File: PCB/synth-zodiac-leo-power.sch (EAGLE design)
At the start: 29 parts, among them J1 2.5 ID x 5.5 OD, J2 HDR-02P

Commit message: Snapshot of designs so far.
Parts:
- removed J1: 2.5 ID x 5.5 OD, con-jack:DC-JACK-2.5MM-REGULAR
- removed J2: HDR-02P, con-headers:CON_02X1-2.54MM-THD-VT
- added 12V: HDR-02P, con-headers:CON_02X1-2.54MM-THD-VT
- added BOOST5: 5V Boost, regulators:BOOST-EN-POLOLU-5V
- added BOOST9, BOOST9N: BOOST 9V, regulators:BOOST-EN-POLOLU-9V
- added CONST: Leo, circuit-monkey-zodiac:CONSTELLATION-LEO
- added GLYPH: Leo, circuit-monkey-zodiac:GLYPH-LEO
- added PCB: PCB FAB, circuit-monkey-zodiac:PENTAGON-40R
- added PWR_AMP, PWR_COW, PWR_EG, PWR_KB, PWR_MIDI, PWR_VCA: (no value), con-jst:04P-VT-SMT
- added VBAT: 2-pin, VT, SMT, con-jst:02PVT-SMT
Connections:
- new net VBAT: VBAT.1
- net +5V: now also PWR_AMP.3, PWR_COW.3, PWR_EG.3, PWR_KB.3, PWR_MIDI.3, PWR_VCA.3
- net +9V: now also PWR_AMP.1, PWR_COW.1, PWR_EG.1, PWR_KB.1, PWR_MIDI.1, PWR_VCA.1
- net -9V: now also PWR_AMP.2, PWR_COW.2, PWR_EG.2, PWR_KB.2, PWR_MIDI.2, PWR_VCA.2
- net GND: now also 12V.2, PCB.GND@1, PWR_AMP.4, PWR_COW.4, PWR_EG.4, PWR_KB.4, PWR_MIDI.4, PWR_VCA.4, VBAT.2; no longer J1.GND, J2.2
- net N$1: now also 12V.1; no longer J1.VIN, J2.1
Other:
- note added: "TODO: - LI-Ion Batt charger - 12V Boost - LEDs - P.Switch Toggle (hole + pads)"
- moved on the sheet: C1, C10, C11, C2, C3, C4, C5, C6, C7, C8, C9, D1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

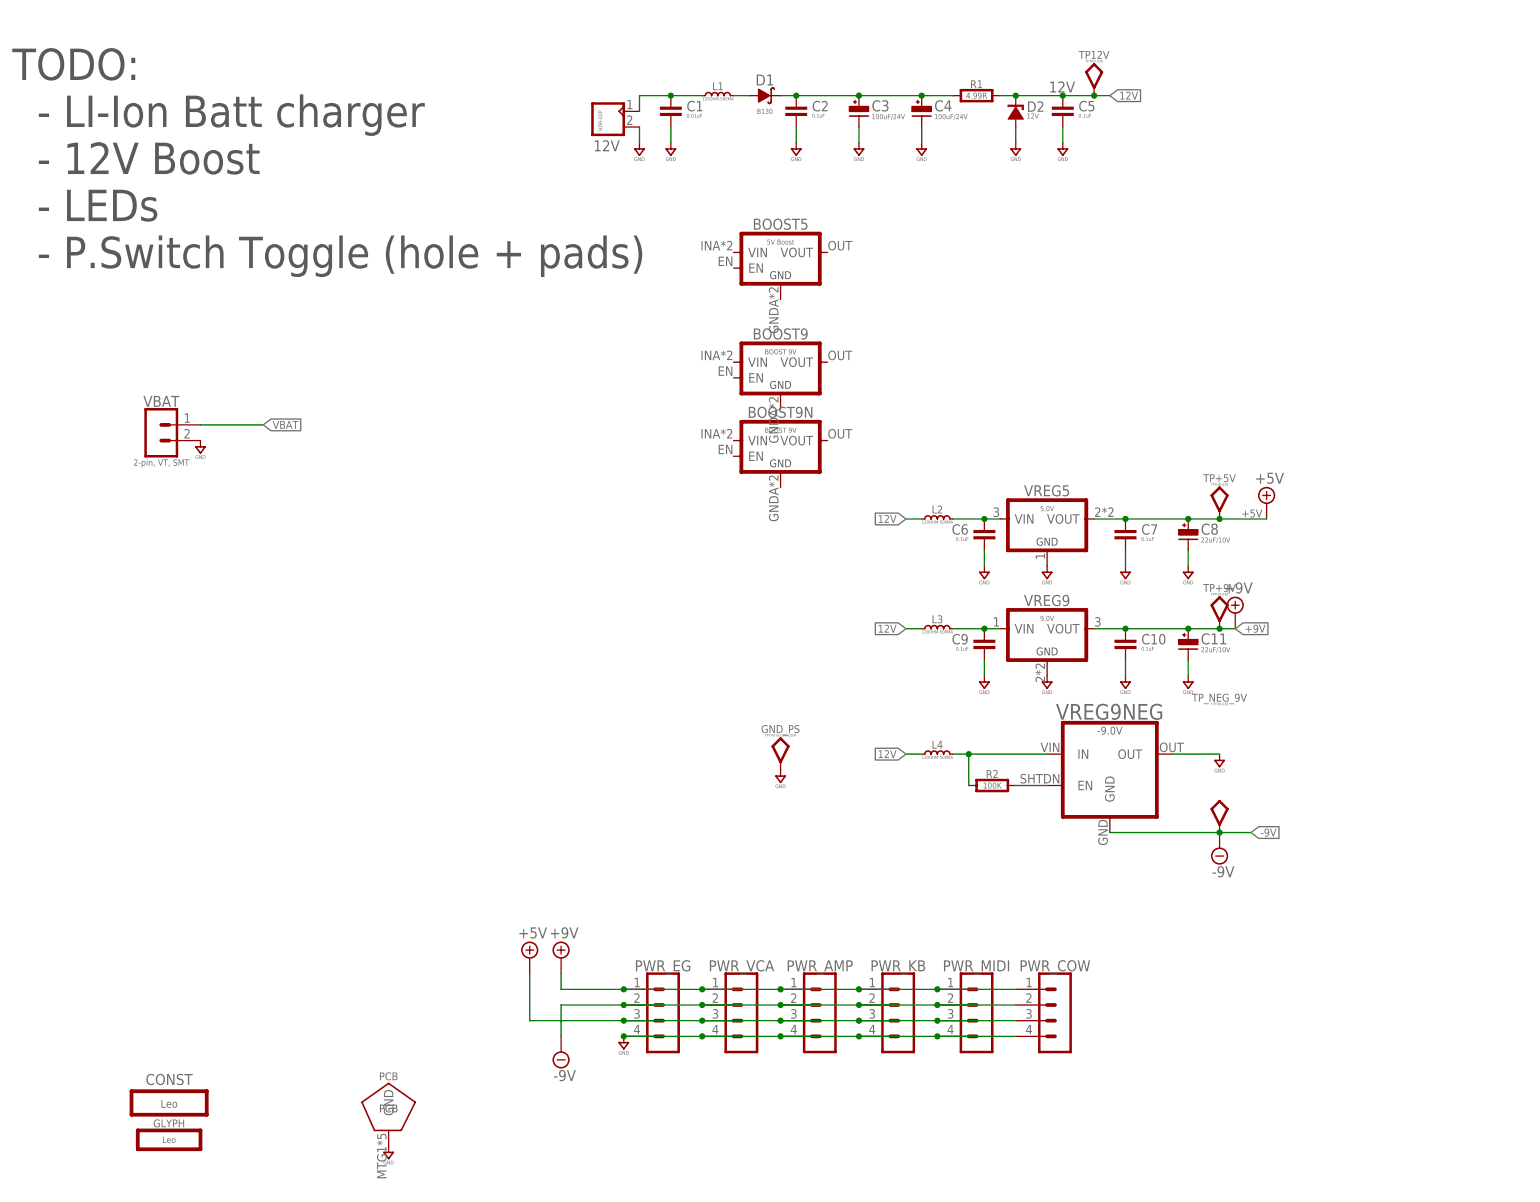
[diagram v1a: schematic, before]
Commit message: Almost ready for FAB.
Sagittarius was mis-spelled, renamed it.  Taurus is still WIP.
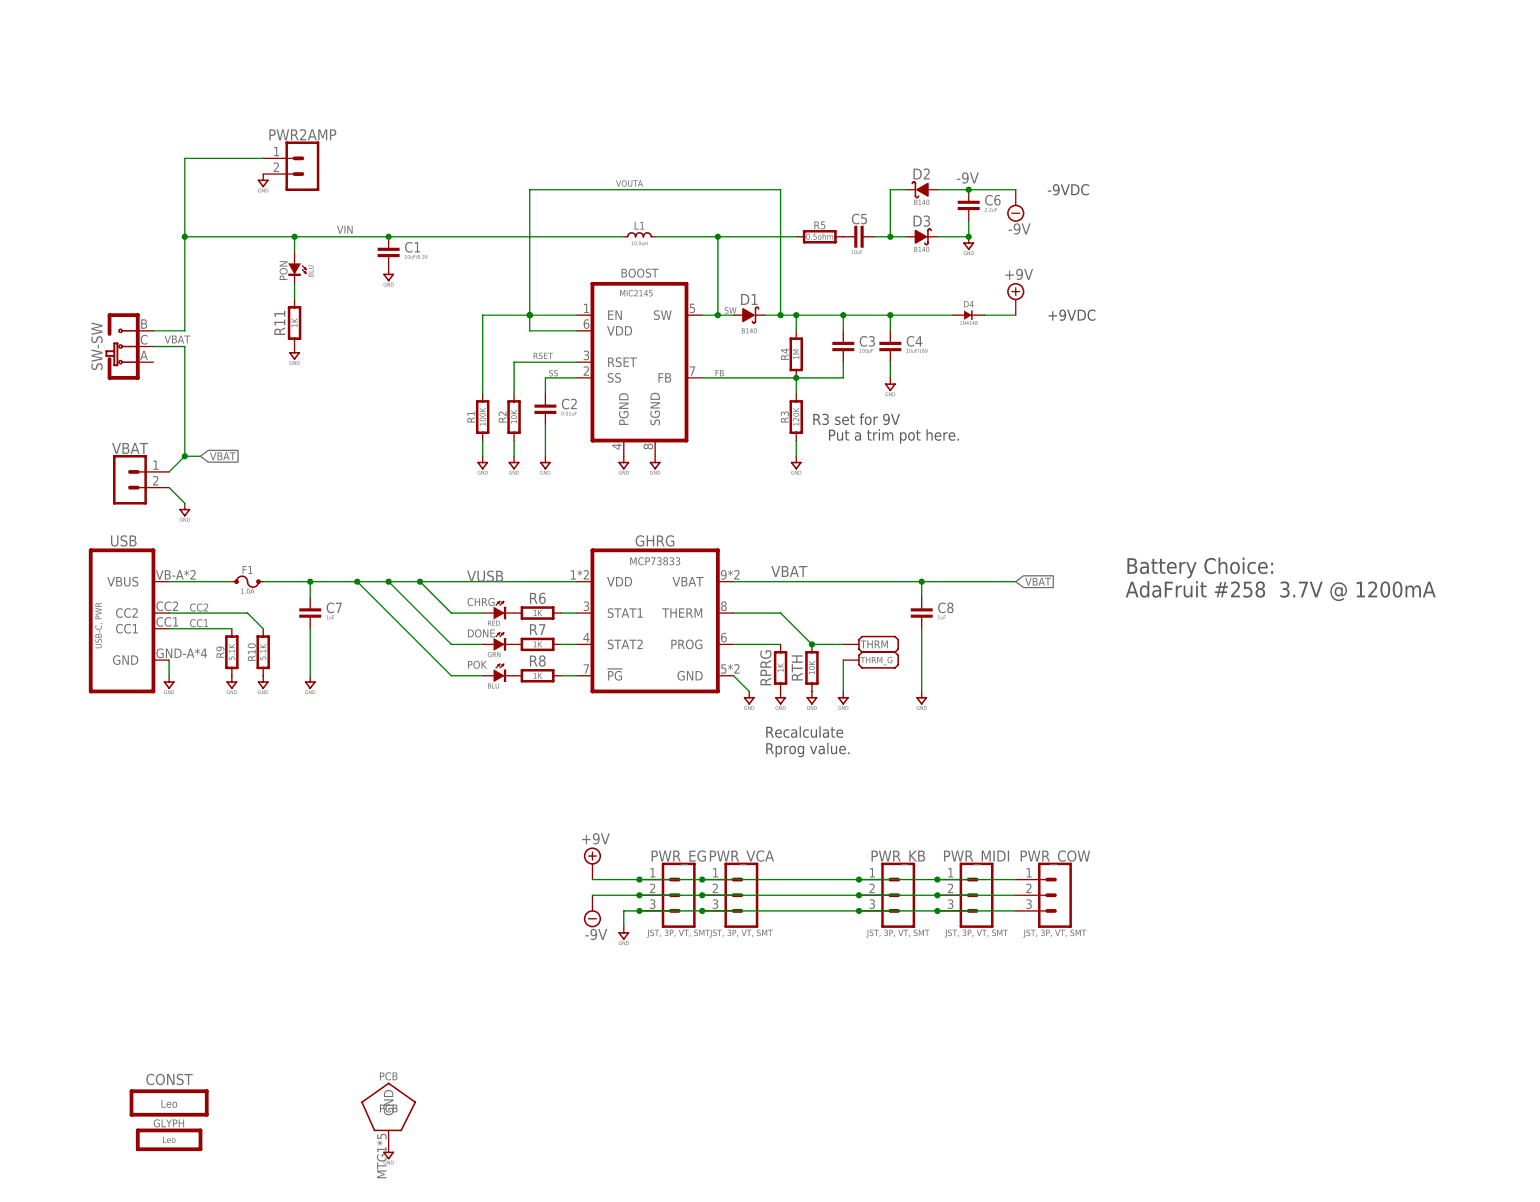
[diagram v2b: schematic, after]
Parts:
- removed 12V: HDR-02P, con-headers:CON_02X1-2.54MM-THD-VT
- removed BOOST5: 5V Boost, regulators:BOOST-EN-POLOLU-5V
- removed BOOST9, BOOST9N: BOOST 9V, regulators:BOOST-EN-POLOLU-9V
- removed C10, C9: 0.1uF, rlc:CAPACITOR0603
- removed C11: 22uF/10V, rlc:CAPACITOR_POL-ALUM-SMT-6.3
- removed GND_PS: TPTHD-SCOPE-LOOP, con-testpoints:TPTHD-SCOPE-LOOP
- removed L2, L3, L4: 120OHM-500MA, rlc:FERRITE120OHM-500MA
- removed PWR_AMP: (no value), con-jst:04P-VT-SMT
- removed TP+5V, TP+9V, TP12V, TP_NEG_9V: TPTHD-038, con-testpoints:TPTHD-038
- removed VREG5: 5.0V, regulators:LDO-3P-1117-5V
- removed VREG9: 9.0V, regulators:LDO-3P--9V
- removed VREG9NEG: -9.0V, regulators:POLOLU-STEPDOWN-4P-9.0V
- added BOOST: MIC2145, regulators:BOOST-MIC2145-MSOP
- added CHRG: RED, led:SMT0603
- added D3: B140, diodes:SCHOTTKYB140
- added D4: 1N4148, diodes:DIODE-1N4148
- added DONE: GRN, led:SMT0603
- added F1: 1.0A, fuse:FUSEBOURNS-MF-MSMF
- added GHRG: MCP73833, co-microchip:MCP73833-DFN
- added POK, PON: BLU, led:SMT0603
- added PWR2AMP: 2-pin, VT, SMT, con-jst:02PVT-SMT
- added R10, R9: 5.1K, rlc:RESISTOR0603
- added R11, R6, R7, R8, RPRG: 1K, rlc:RESISTOR0603
- added R3: 120K, rlc:RESISTOR0603
- added R4: 1M, rlc:RESISTOR0603
- added R5: 0.5ohm, rlc:RESISTOR0603
- added RTH: 10K, rlc:RESISTOR0603
- added SW: (no value), switch-thd:SLIDE-SPDTSS-12-F45-TH-PCB
- added THRM, THRM_G: PADSMD-050X050, con-testpoints:PADSMD-050X050
- added USB: USB-C, PWR, con-usb:USB-C-PWR-SMT-PNL
- C1: value 0.01uF -> 10uF/6.3V
- C2: value 0.1uF -> 0.01uF
- C3: value 100uF/24V -> 100pF; device rlc:CAPACITOR_POL-ALUM-SMT-6.3 -> rlc:CAPACITOR0603; COST01 0.5 -> (none); COST10 0.5 -> (none); COST100 0.4 -> (none); MFR Wurth -> (none); MPN 865090445008 -> (none)
- C4: value 100uF/24V -> 10uF/16V; device rlc:CAPACITOR_POL-ALUM-SMT-6.3 -> rlc:CAPACITOR0603; COST01 0.5 -> (none); COST10 0.5 -> (none); COST100 0.4 -> (none); MFR Wurth -> (none); MPN 865090445008 -> (none)
- C5: value 0.1uF -> 10uF
- C6: value 0.1uF -> 2.2uF
- C7: value 0.1uF -> 1uF
- C8: value 22uF/10V -> 1uF; device rlc:CAPACITOR_POL-ALUM-SMT-6.3 -> rlc:CAPACITOR0603; COST01 0.5 -> (none); COST10 0.5 -> (none); COST100 0.4 -> (none); MFR Wurth -> (none); MPN 865090445008 -> (none)
- D1: value B130 -> B140; device diodes:SCHOTTKYB130 -> diodes:SCHOTTKYB140
- D2: value 12V -> B140; device diodes:ZENERSOT-23 -> diodes:SCHOTTKYB140; COST01 0.44 -> (none); COST10 0.34 -> (none); COST100 0.20 -> (none); MFR ROHM -> (none); MPN BZX84B12VLYT116 -> (none)
- L1: value 120OHM-500MA -> 10.0uH; device rlc:FERRITE120OHM-500MA -> rlc:INDUCTORSMD-05X04MM; MPN BLM18SP102SN1D -> (none)
- PWR_COW, PWR_EG, PWR_KB, PWR_MIDI, PWR_VCA: value (none) -> JST, 3P, VT, SMT; device con-jst:04P-VT-SMT -> con-jst:03P-VT-SMT
- R1: value 4.99R -> 100K; device rlc:RESISTOR1206 -> rlc:RESISTOR0603
- R2: value 100K -> 10K
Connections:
- removed net +5V: C7.1, C8.P, PWR_AMP.3, PWR_COW.3, PWR_EG.3, PWR_KB.3, PWR_MIDI.3, PWR_VCA.3, TP+5V.P$1, VREG5.VOUT
- removed net 12V: C5.1, D2.K, L2.1, L3.1, L4.1, R1.2, TP12V.P$1
- new net CC1: R9.2, USB.CC1
- new net CC2: R10.2, USB.CC2
- new net FB: BOOST.FB, C3.2, R3.2, R4.1
- new net N$10: GHRG.STAT2, R7.2
- new net N$11: GHRG.!PG, R8.2
- new net N$12: GHRG.THERM, RTH.2, THRM.PAD
- new net N$8: GHRG.PROG, RPRG.2
- new net N$9: GHRG.STAT1, R6.2
- new net RSET: BOOST.RSET, R2.2
- new net SS: BOOST.SS, C2.1
- new net SW: BOOST.SW, D1.A, L1.P$1, R5.1
- new net VIN: C1.1, L1.P$2, PON.A, PWR2AMP.1, SW-SW.B
- new net VOUTA: BOOST.EN, BOOST.VDD, C3.1, C4.1, D1.K, D4.A, R1.2, R4.2
- new net VUSB: C7.1, CHRG.A, DONE.A, F1.2, GHRG.VDD, POK.A
- net +9V: now also D4.K; no longer C10.1, C11.P, PWR_AMP.1, TP+9V.P$1, VREG9.VOUT
- net -9V: now also C6.1, D2.A; no longer PWR_AMP.2, TP_NEG_9V.P$1, VREG9NEG.GND
- net GND: now also BOOST.PGND, BOOST.SGND, C4.2, C8.2, D3.K, GHRG.GND, PWR2AMP.2, PWR_COW.3, PWR_EG.3, PWR_KB.3, PWR_MIDI.3, PWR_VCA.3, R1.1, R10.1, R11.1, R2.1, R3.1, R9.1, RPRG.1, RTH.1, THRM_G.PAD, USB.GND; no longer 12V.2, C10.2, C11.N, C3.N, C4.N, C5.2, C8.N, C9.2, D2.A, GND_PS.P$1, PWR_AMP.4, PWR_COW.4, PWR_EG.4, PWR_KB.4, PWR_MIDI.4, PWR_VCA.4, VREG5.GND, VREG9.GND, VREG9NEG.OUT
- net N$1: now also C5.1, R5.2; no longer 12V.1, C1.1, L1.1
- net N$2: now also C5.2, D2.K, D3.A; no longer D1.A, L1.2
- net N$3: now also CHRG.C, R6.1; no longer C2.1, C3.P, C4.P, D1.K, R1.1
- net N$4: now also PON.C, R11.2; no longer C9.1, L3.2, VREG9.VIN
- net N$5: now also DONE.C, R7.1; no longer C6.1, L2.2, VREG5.VIN
- net N$6: now also F1.1, USB.VBUS; no longer L4.2, R2.1, VREG9NEG.IN
- net N$7: now also POK.C, R8.1; no longer R2.2, VREG9NEG.EN
- net VBAT: now also C8.1, GHRG.VBAT, SW-SW.C
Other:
- note added: "+9VDC"
- note added: "-9VDC"
- note added: "Battery Choice: AdaFruit #258 3.7V @ 1200mA"
- note added: "Put a trim pot here."
- note added: "R3 set for 9V"
- note added: "Recalculate Rprog value."
- note removed: "TODO: - LI-Ion Batt charger - 12V Boost - LEDs - P.Switch Toggle (hole + pads)"
- moved on the sheet: C1, C2, C5, C6, C7, D1, R1, R2, VBAT

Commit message: Work in progress for rev A,  VCO rev.B
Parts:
- removed PWR2AMP, VBAT: 2-pin, VT, SMT, con-jst:02PVT-SMT
- removed PWR_COW, PWR_EG, PWR_KB, PWR_MIDI, PWR_VCA: JST, 3P, VT, SMT, con-jst:03P-VT-SMT
- removed SW: (no value), switch-thd:SLIDE-SPDTSS-12-F45-TH-PCB
- added BATT, V2AMP, V2LED: JST, SH, 2P, con-jst:02P-SM-VT-SMT
- added PWR: (no value), switch-thd:SLIDE-SPDT-MNTSS-12-F45-TH-PCB
- added PWR01, PWR02, PWR03, PWR04, PWR05, PWR06, PWR07, PWR08, PWR09, PWR10, PWR11: JST SM 3P, con-jst:03P-SM-VT-SMT
- F1: value 1.0A -> 0.5A
- USB: value USB-C, PWR -> USB, POWER; device con-usb:USB-C-PWR-SMT-PNL -> con-usb:USB-C-PWRGCT-4515
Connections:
- net N$6 renamed VBUS
- net +9V: now also PWR01.1, PWR02.1, PWR03.1, PWR04.1, PWR05.1, PWR06.1, PWR07.1, PWR08.1, PWR09.1, PWR10.1, PWR11.1; no longer PWR_COW.1, PWR_EG.1, PWR_KB.1, PWR_MIDI.1, PWR_VCA.1
- net -9V: now also PWR01.2, PWR02.2, PWR03.2, PWR04.2, PWR05.2, PWR06.2, PWR07.2, PWR08.2, PWR09.2, PWR10.2, PWR11.2; no longer PWR_COW.2, PWR_EG.2, PWR_KB.2, PWR_MIDI.2, PWR_VCA.2
- net GND: now also BATT.2, PWR01.3, PWR02.3, PWR03.3, PWR04.3, PWR05.3, PWR06.3, PWR07.3, PWR08.3, PWR09.3, PWR10.3, PWR11.3, V2AMP.2, V2LED.2; no longer PWR2AMP.2, PWR_COW.3, PWR_EG.3, PWR_KB.3, PWR_MIDI.3, PWR_VCA.3, VBAT.2
- net VBAT: now also BATT.1, PWR-SW.A; no longer SW-SW.C, VBAT.1
- net VIN: now also PWR-SW.C, V2AMP.1, V2LED.1; no longer PWR2AMP.1, SW-SW.B
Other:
- note added: "Leo"
- note added: "Power"
- note added: "SATAN'S CYCLE WORKS"
- note added: "Zodiac Synth"
- moved on the sheet: BOOST, C1, C2, C3, C4, C5, C6, C7, C8, CHRG, D1, D2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

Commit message: Perhaps final Rev. A?
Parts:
- PWR: device switch-thd:SLIDE-SPDT-MNTSS-12-F45-TH-PCB -> switch-thd:SLIDE-SPDT-MNTSS-12-F45-TH-PCB-2
- USB: value USB, POWER -> USB-C, POWER
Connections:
- net VBAT: now also PWR-SW.B; no longer PWR-SW.A
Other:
- moved on the sheet: PWR-SW

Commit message: Tune values and some schematic visual tweaks.
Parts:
- C4: value 10uF/16V -> 10uF/25V
- C5: value 10uF -> 10uF/25V
- C6: value 2.2uF -> 2.2uF/16V
- C7, C8: value 1uF -> 1uF/10V
- R3: value 120K -> 143K
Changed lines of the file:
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@@
 <part name="R2" library="rlc" library_urn="urn:adsk.eagle:library:4192893" deviceset="RESISTOR" device="0603" package3d_urn="urn:adsk.eagle:package:4193040/5" value="10K"/>
 <part name="C3" library="rlc" library_urn="urn:adsk.eagle:library:4192893" deviceset="CAPACITOR" device="0603" package3d_urn="urn:adsk.eagle:package:4193021/5" value="100pF"/>
-<part name="R3" library="rlc" library_urn="urn:adsk.eagle:library:4192893" deviceset="RESISTOR" device="0603" package3d_urn="urn:adsk.eagle:package:4193040/5" value="120K"/>
+<part name="R3" library="rlc" library_urn="urn:adsk.eagle:library:4192893" deviceset="RESISTOR" device="0603" package3d_urn="urn:adsk.eagle:package:4193040/5" value="143K"/>
 <part name="R4" library="rlc" library_urn="urn:adsk.eagle:library:4192893" deviceset="RESISTOR" device="0603" package3d_urn="urn:adsk.eagle:package:4193040/5" value="1M"/>
-<part name="C4" library="rlc" library_urn="urn:adsk.eagle:library:4192893" deviceset="CAPACITOR" device="0603" package3d_urn="urn:adsk.eagle:package:4193021/5" value="10uF/16V"/>
+<part name="C4" library="rlc" library_urn="urn:adsk.eagle:library:4192893" deviceset="CAPACITOR" device="0603" package3d_urn="urn:adsk.eagle:package:4193021/5" value="10uF/25V"/>
 <part name="SUPPLY2" library="supply" library_urn="urn:adsk.eagle:library:10485988" deviceset="GND" device=""/>
 <part name="SUPPLY3" library="supply" library_urn="urn:adsk.eagle:library:10485988" deviceset="GND" device=""/>
@@
 <part name="D2" library="diodes" library_urn="urn:adsk.eagle:library:7189447" deviceset="SCHOTTKY" device="B140" package3d_urn="urn:adsk.eagle:package:7189483/2" value="B140"/>
 <part name="D3" library="diodes" library_urn="urn:adsk.eagle:library:7189447" deviceset="SCHOTTKY" device="B140" package3d_urn="urn:adsk.eagle:package:7189483/2" value="B140"/>
-<part name="C5" library="rlc" library_urn="urn:adsk.eagle:library:4192893" deviceset="CAPACITOR" device="0603" package3d_urn="urn:adsk.eagle:package:4193021/5" value="10uF"/>
+<part name="C5" library="rlc" library_urn="urn:adsk.eagle:library:4192893" deviceset="CAPACITOR" device="0603" package3d_urn="urn:adsk.eagle:package:4193021/5" value="10uF/25V"/>
 <part name="SUPPLY9" library="supply" library_urn="urn:adsk.eagle:library:10485988" deviceset="GND" device=""/>
-<part name="C6" library="rlc" library_urn="urn:adsk.eagle:library:4192893" deviceset="CAPACITOR" device="0603" package3d_urn="urn:adsk.eagle:package:4193021/5" value="2.2uF"/>
+<part name="C6" library="rlc" library_urn="urn:adsk.eagle:library:4192893" deviceset="CAPACITOR" device="0603" package3d_urn="urn:adsk.eagle:package:4193021/5" value="2.2uF/16V"/>
 <part name="D4" library="diodes" library_urn="urn:adsk.eagle:library:7189447" deviceset="DIODE-" device="1N4148" package3d_urn="urn:adsk.eagle:package:7189471/3" value="1N4148"/>
-<part name="C7" library="rlc" library_urn="urn:adsk.eagle:library:4192893" deviceset="CAPACITOR" device="0603" package3d_urn="urn:adsk.eagle:package:4193021/5" value="1uF"/>
+<part name="C7" library="rlc" library_urn="urn:adsk.eagle:library:4192893" deviceset="CAPACITOR" device="0603" package3d_urn="urn:adsk.eagle:package:4193021/5" value="1uF/10V"/>
 <part name="GHRG" library="co-microchip" library_urn="urn:adsk.eagle:library:9738997" deviceset="MCP73833" device="-DFN" package3d_urn="urn:adsk.eagle:package:9739049/3" value="MCP73833"/>
 <part name="R6" library="rlc" library_urn="urn:adsk.eagle:library:4192893" deviceset="RESISTOR" device="0603" package3d_urn="urn:adsk.eagle:package:4193040/5" value="1K"/>
@@
 <part name="POK" library="led" library_urn="urn:adsk.eagle:library:5499911" deviceset="SMT" device="0603" package3d_urn="urn:adsk.eagle:package:5499947/3" value="BLU"/>
 <part name="R8" library="rlc" library_urn="urn:adsk.eagle:library:4192893" deviceset="RESISTOR" device="0603" package3d_urn="urn:adsk.eagle:package:4193040/5" value="1K"/>
-<part name="C8" library="rlc" library_urn="urn:adsk.eagle:library:4192893" deviceset="CAPACITOR" device="0603" package3d_urn="urn:adsk.eagle:package:4193021/5" value="1uF"/>
+<part name="C8" library="rlc" library_urn="urn:adsk.eagle:library:4192893" deviceset="CAPACITOR" device="0603" package3d_urn="urn:adsk.eagle:package:4193021/5" value="1uF/10V"/>
 <part name="RPRG" library="rlc" library_urn="urn:adsk.eagle:library:4192893" deviceset="RESISTOR" device="0603" package3d_urn="urn:adsk.eagle:package:4193040/5" value="1K"/>
 <part name="RTH" library="rlc" library_urn="urn:adsk.eagle:library:4192893" deviceset="RESISTOR" device="0603" package3d_urn="urn:adsk.eagle:package:4193040/5" value="10K"/>
